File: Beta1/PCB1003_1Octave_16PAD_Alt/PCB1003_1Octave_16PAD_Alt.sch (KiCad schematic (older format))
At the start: 93 parts, among them P0 CONN_01X01, P1 CONN_01X01, P10 CONN_01X01, P100 CONN_01X01, P101 CONN_01X01, P102 CONN_01X01, P103 CONN_01X01, P104 CONN_01X01, P105 CONN_01X01, P106 CONN_01X01, P107 CONN_01X01, P108 CONN_01X01, P109 CONN_01X01, P11 CONN_01X01, P110 CONN_01X01, P111 CONN_01X01, P2 CONN_01X01, P200 CONN_01X01, P201 CONN_01X01, P202 CONN_01X01, P203 CONN_01X01, P204 CONN_01X01, P205 CONN_01X01, P206 CONN_01X01, P207 CONN_01X01, P208 CONN_01X01, P209 CONN_01X01, P210 CONN_01X01, P211 CONN_01X01, P3 CONN_01X01, P4 CONN_01X01, P5 CONN_01X01, P6 CONN_01X01, P7 CONN_01X01, P8 CONN_01X01, P9 CONN_01X01, U1 CPT112S, U100 CPT112S, U200 CPT112S

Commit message: Pin swap reroute WIP.
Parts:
- PAD2: footprint Liberry:TOUCH_PAD_10CM -> Liberry:TOUCH_PAD_10CM_V2
- renumbered PAD8 to PD0, PAD9 to PD1, PAD108 to PD100, PAD109 to PD101, PAD110 to PD102, PAD111 to PD103, PAD10 to PD2, PAD11 to PD3, P0 to TP0, P1 to TP1, P10 to TP10, P100 to TP100, P101 to TP101, P102 to TP102, P103 to TP103, P104 to TP104, P105 to TP105, P106 to TP106, P107 to TP107, P108 to TP108, P109 to TP109, P11 to TP11, P110 to TP110, P111 to TP111, P2 to TP2, P200 to TP200, P201 to TP201, P202 to TP202, P203 to TP203, P204 to TP204, P205 to TP205, P206 to TP206, P207 to TP207, P208 to TP208, P209 to TP209, P210 to TP210, P211 to TP211, P3 to TP3, P4 to TP4, P5 to TP5, P6 to TP6, P7 to TP7, P8 to TP8, P9 to TP9
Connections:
- net labels added: CHIP_04, CHIP_05, CHIP_06, CHIP_07, CHIP_08, CHIP_09, CHIP_10, CHIP_104, CHIP_105, CHIP_106, CHIP_107, CHIP_108, CHIP_109, CHIP_11, CHIP_110, CHIP_111, CHIP_200, CHIP_201, CHIP_202, CHIP_203, CHIP_204, CHIP_205, CHIP_206, CHIP_207, CHIP_208, CHIP_209, CHIP_210, CHIP_211
- net labels removed: PAD0, PAD1, PAD2, PAD3, PAD4, PAD5, PAD6, PAD7
- wire segments 240 -> 194
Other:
- note added: "The Pad to Chip connections are backdriven by the physics of the capacitance touch-chip. \nIn order to minimize interference between traces, we must alternate them. \nThe low cost of the sensor and it's suitability in a field of competitors, \ncoupled with the chip configuration tradeoffs to achieve HMI realtime feel \nrequires that we break best practice of making the data labels match the bit o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"
- moved on the sheet: PAD0, PAD1, PAD100, PAD101, PAD102, PAD103, PAD104, PAD105, PAD106, PAD107, PAD2, PAD3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

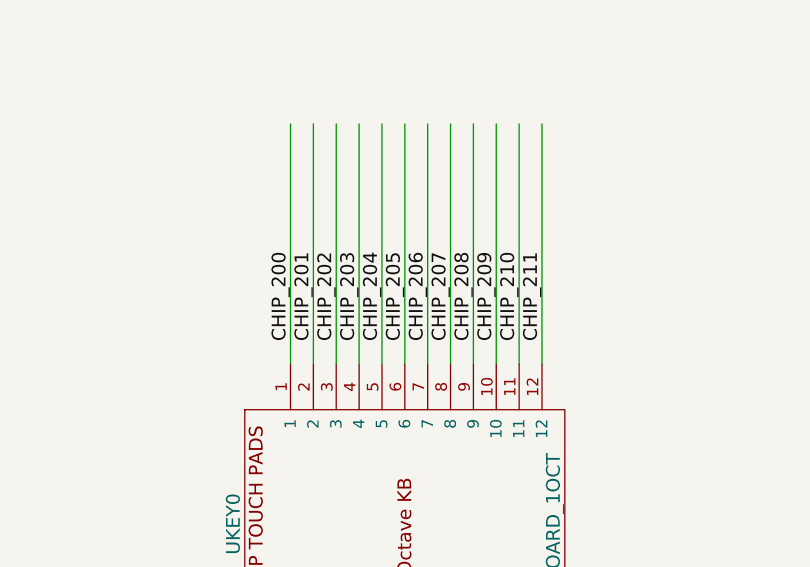
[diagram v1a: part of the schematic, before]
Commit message: Reroute WIP; Pads are off-screen
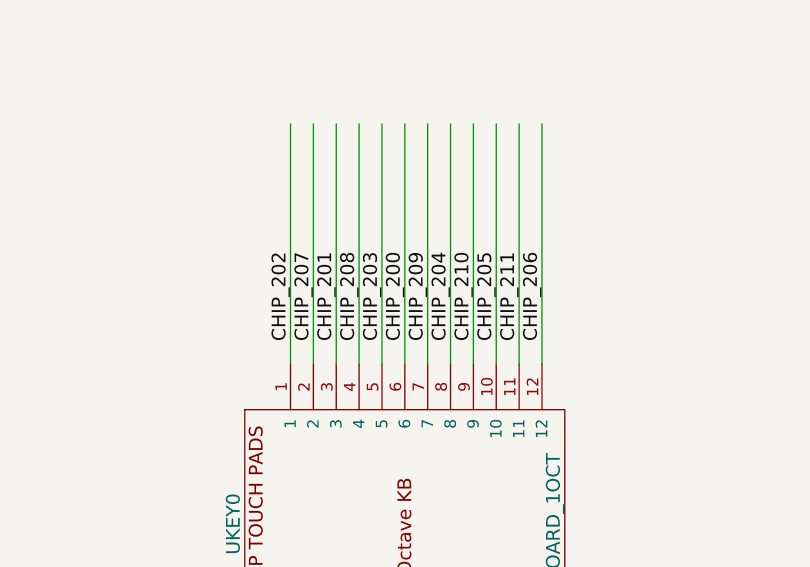
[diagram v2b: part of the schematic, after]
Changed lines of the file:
@@
 	10450 15650 10450 14600
 Text Label 10450 15550 1    60   ~ 0
-CHIP_200
+CHIP_202
 Wire Wire Line
 	10550 15650 10550 14600
 Text Label 10550 15550 1    60   ~ 0
-CHIP_201
+CHIP_207
 Wire Wire Line
 	10650 15650 10650 14600
 Text Label 10650 15550 1    60   ~ 0
-CHIP_202
+CHIP_201
 Wire Wire Line
 	10750 15650 10750 14600
 Text Label 10750 15550 1    60   ~ 0
-CHIP_203
+CHIP_208
 Wire Wire Line
 	10850 15650 10850 14600
 Text Label 10850 15550 1    60   ~ 0
-CHIP_204
+CHIP_203
 Wire Wire Line
 	10950 15650 10950 14600
 Text Label 10950 15550 1    60   ~ 0
-CHIP_205
+CHIP_200
 Wire Wire Line
 	11050 15650 11050 14600
 Text Label 11050 15550 1    60   ~ 0
-CHIP_206
+CHIP_209
 Wire Wire Line
 	11150 15650 11150 14600
 Text Label 11150 15550 1    60   ~ 0
-CHIP_207
+CHIP_204
 Wire Wire Line
 	11250 15650 11250 14600
 Text Label 11250 15550 1    60   ~ 0
-CHIP_208
+CHIP_210
 Wire Wire Line
 	11350 15650 11350 14600
 Text Label 11350 15550 1    60   ~ 0
-CHIP_209
+CHIP_205
 Wire Wire Line
 	11450 15650 11450 14600
 Text Label 11450 15550 1    60   ~ 0
-CHIP_210
+CHIP_211
 Wire Wire Line
 	11550 15650 11550 14600
 Text Label 11550 15550 1    60   ~ 0
-CHIP_211
+CHIP_206
 $EndSCHEMATC

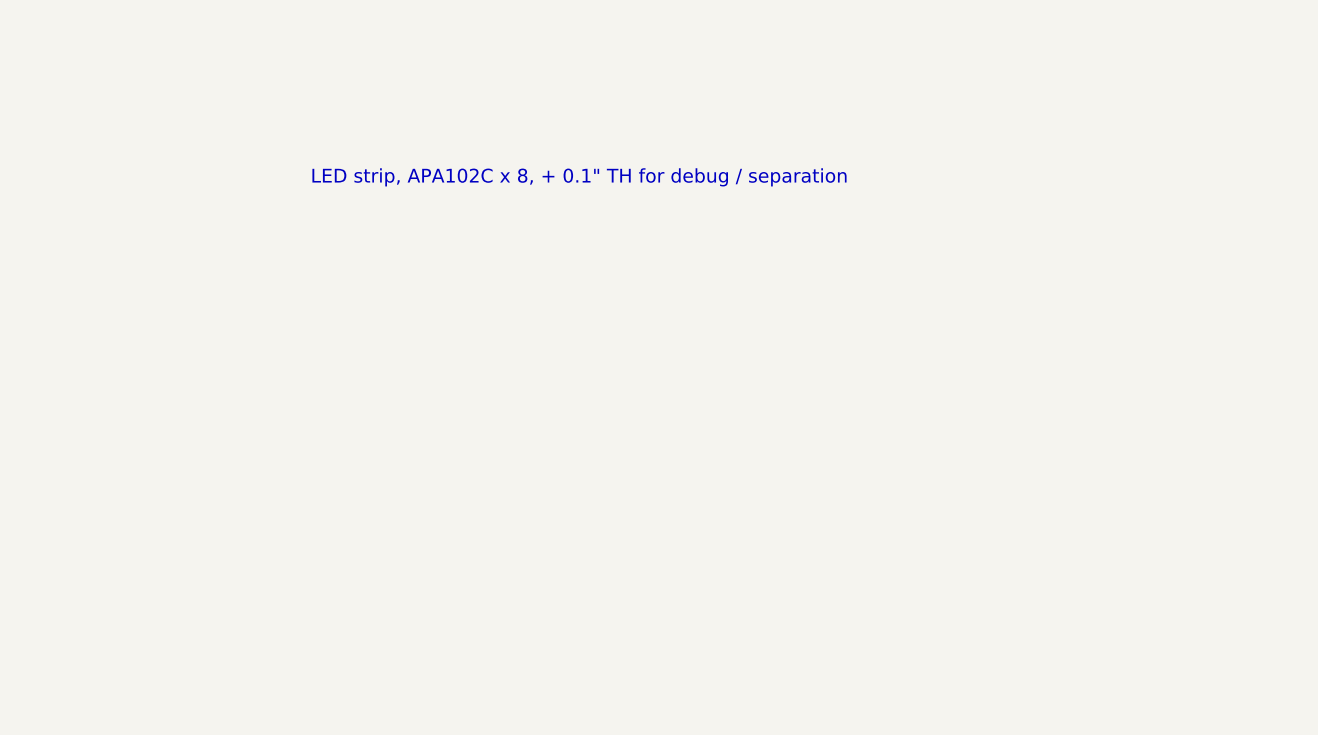
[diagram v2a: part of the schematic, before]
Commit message: Added flavor text to schematic
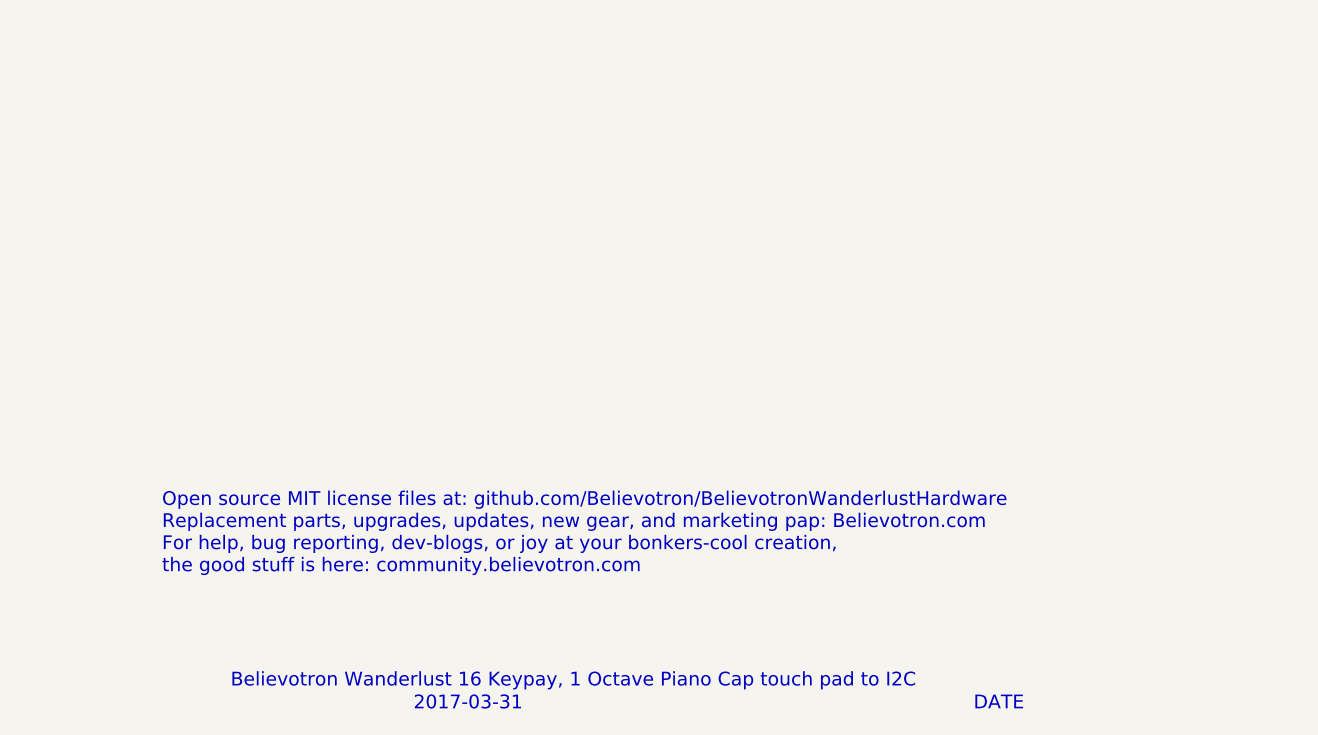
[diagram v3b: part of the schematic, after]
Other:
- note added: "2017-03-31"
- note added: "Believotron Wanderlust 16 Keypay, 1 Octave Piano Cap touch pad to I2C"
- note added: "DATE"
- note added: "Open source MIT license files at: github.com/Believotron/BelievotronWanderlustHardware\nReplacement parts, upgrades, updates, new gear, and marketing pap: Believotron.com\nFor help, bug reporting, dev-blogs, or joy at your bonkers-cool creation, \nthe good stuff is here: community.believotron.com\n"
- note removed: "LED strip, APA102C x 8, + 0.1" TH for debug / separation"
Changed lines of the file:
@@
 Comment4 ""
 $EndDescr
-Text Notes 30000 19050 0    60   ~ 0
-LED strip, APA102C x 8, + 0.1" TH for debug / separation
 $Comp
 L +3.3V #PWR01
@@
 Text Label 11550 15550 1    60   ~ 0
 CHIP_206
+Text Notes 29350 20750 0    60   ~ 0
+Open source MIT license files at: github.com/Believotron/BelievotronWanderlustHardware\nReplacement parts, upgrades, updates, new gear, and marketing pap: Believotron.com\nFor help, bug reporting, dev-blogs, or joy at your bonkers-cool creation, \nthe good stuff is here: community.believotron.com\n
+Text Notes 30450 21350 0    60   ~ 0
+2017-03-31
+Text Notes 32900 21350 0    60   ~ 0
+DATE
+Text Notes 29650 21250 0    60   ~ 0
+Believotron Wanderlust 16 Keypay, 1 Octave Piano Cap touch pad to I2C
 $EndSCHEMATC
